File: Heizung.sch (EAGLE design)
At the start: 32 parts, among them IC1 MEGA8-PTQFP, Q2 2N7002, Q3 2N7002

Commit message: change min width to 3.5mm, fix XTAL
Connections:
- new net N$41: J_1.1, J_2.1, J_3.1, J_4.1
- net GND: no longer J_1.1, J_2.1, J_3.1, J_4.1
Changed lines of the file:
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@@
 <grid distance="0.1" unitdist="inch" unit="inch" style="lines" multiple="1" display="no" altdistance="0.01" altunitdist="inch" altunit="inch"/>
 <layers>
-<layer number="1" name="Top" color="4" fill="1" visible="no" active="no"/>
-<layer number="16" name="Bottom" color="1" fill="1" visible="no" active="no"/>
-<layer number="17" name="Pads" color="2" fill="1" visible="no" active="no"/>
-<layer number="18" name="Vias" color="2" fill="1" visible="no" active="no"/>
-<layer number="19" name="Unrouted" color="6" fill="1" visible="no" active="no"/>
-<layer number="20" name="Dimension" color="15" fill="1" visible="no" active="no"/>
-<layer number="21" name="tPlace" color="7" fill="1" visible="no" active="no"/>
-<layer number="22" name="bPlace" color="7" fill="1" visible="no" active="no"/>
-<layer number="23" name="tOrigins" color="15" fill="1" visible="no" active="no"/>
-<layer number="24" name="bOrigins" color="15" fill="1" visible="no" active="no"/>
-<layer number="25" name="tNames" color="7" fill="1" visible="no" active="no"/>
-<layer number="26" name="bNames" color="7" fill="1" visible="no" active="no"/>
-<layer number="27" name="tValues" color="7" fill="1" visible="no" active="no"/>
-<layer number="28" name="bValues" color="7" fill="1" visible="no" active="no"/>
+<layer number="1" name="Top" color="4" fill="1" visible="yes" active="no"/>
+<layer number="16" name="Bottom" color="1" fill="1" visible="yes" active="no"/>
+<layer number="17" name="Pads" color="2" fill="1" visible="yes" active="no"/>
+<layer number="18" name="Vias" color="2" fill="1" visible="yes" active="no"/>
+<layer number="19" name="Unrouted" color="6" fill="1" visible="yes" active="no"/>
+<layer number="20" name="Dimension" color="15" fill="1" visible="yes" active="no"/>
+<layer number="21" name="tPlace" color="7" fill="1" visible="yes" active="no"/>
+<layer number="22" name="bPlace" color="7" fill="1" visible="yes" active="no"/>
+<layer number="23" name="tOrigins" color="15" fill="1" visible="yes" active="no"/>
+<layer number="24" name="bOrigins" color="15" fill="1" visible="yes" active="no"/>
+<layer number="25" name="tNames" color="7" fill="1" visible="yes" active="no"/>
+<layer number="26" name="bNames" color="7" fill="1" visible="yes" active="no"/>
+<layer number="27" name="tValues" color="7" fill="1" visible="yes" active="no"/>
+<layer number="28" name="bValues" color="7" fill="1" visible="yes" active="no"/>
 <layer number="29" name="tStop" color="7" fill="3" visible="no" active="no"/>
 <layer number="30" name="bStop" color="7" fill="6" visible="no" active="no"/>
@@
 <layer number="35" name="tGlue" color="7" fill="4" visible="no" active="no"/>
 <layer number="36" name="bGlue" color="7" fill="5" visible="no" active="no"/>
-<layer number="37" name="tTest" color="7" fill="1" visible="no" active="no"/>
-<layer number="38" name="bTest" color="7" fill="1" visible="no" active="no"/>
+<layer number="37" name="tTest" color="7" fill="1" visible="yes" active="no"/>
+<layer number="38" name="bTest" color="7" fill="1" visible="yes" active="no"/>
 <layer number="39" name="tKeepout" color="4" fill="11" visible="no" active="no"/>
 <layer number="40" name="bKeepout" color="1" fill="11" visible="no" active="no"/>
@@
 <layer number="44" name="Drills" color="7" fill="1" visible="no" active="no"/>
 <layer number="45" name="Holes" color="7" fill="1" visible="no" active="no"/>
-<layer number="46" name="Milling" color="3" fill="1" visible="no" active="no"/>
-<layer number="47" name="Measures" color="7" fill="1" visible="no" active="no"/>
-<layer number="48" name="Document" color="7" fill="1" visible="no" active="no"/>
-<layer number="49" name="Reference" color="7" fill="1" visible="no" active="no"/>
-<layer number="50" name="dxf" color="7" fill="1" visible="no" active="no"/>
-<layer number="51" name="tDocu" color="7" fill="1" visible="no" active="no"/>
-<layer number="52" name="bDocu" color="7" fill="1" visible="no" active="no"/>
-<layer number="53" name="tGND_GNDA" color="7" fill="9" visible="no" active="no"/>
-<layer number="54" name="bGND_GNDA" color="1" fill="9" visible="no" active="no"/>
-<layer number="56" name="wert" color="7" fill="1" visible="no" active="no"/>
-<layer number="57" name="tCAD" color="7" fill="1" visible="no" active="no"/>
+<layer number="46" name="Milling" color="3" fill="1" visible="yes" active="no"/>
+<layer number="47" name="Measures" color="7" fill="1" visible="yes" active="no"/>
+<layer number="48" name="Document" color="7" fill="1" visible="yes" active="no"/>
+<layer number="49" name="Reference" color="7" fill="1" visible="yes" active="no"/>
+<layer number="50" name="dxf" color="7" fill="1" visible="yes" active="no"/>
+<layer number="51" name="tDocu" color="7" fill="1" visible="yes" active="no"/>
+<layer number="52" name="bDocu" color="7" fill="1" visible="yes" active="no"/>
+<layer number="53" name="tGND_GNDA" color="7" fill="9" visible="yes" active="no"/>
+<layer number="54" name="bGND_GNDA" color="1" fill="9" visible="yes" active="no"/>
+<layer number="56" name="wert" color="7" fill="1" visible="yes" active="no"/>
+<layer number="57" name="tCAD" color="7" fill="1" visible="yes" active="no"/>
 <layer number="90" name="Modules" color="5" fill="1" visible="yes" active="yes"/>
 <layer number="91" name="Nets" color="2" fill="1" visible="yes" active="yes"/>
@@
 <junction x="63.5" y="78.74"/>
 <pinref part="GND_" gate="G$1" pin="1"/>
-<wire x1="142.24" y1="81.28" x2="142.24" y2="88.9" width="0.1524" layer="91"/>
+<wire x1="142.24" y1="78.74" x2="142.24" y2="88.9" width="0.1524" layer="91"/>
 <pinref part="GND1" gate="G$1" pin="1"/>
 <wire x1="142.24" y1="88.9" x2="142.24" y2="106.68" width="0.1524" layer="91"/>
@@
 <wire x1="20.32" y1="99.06" x2="12.7" y2="99.06" width="0.1524" layer="91"/>
 <junction x="12.7" y="99.06"/>
-<wire x1="142.24" y1="78.74" x2="142.24" y2="81.28" width="0.1524" layer="91"/>
-<wire x1="142.24" y1="81.28" x2="165.1" y2="81.28" width="0.1524" layer="91"/>
-<pinref part="J_4" gate="G$1" pin="1"/>
-<wire x1="165.1" y1="81.28" x2="165.1" y2="76.2" width="0.1524" layer="91"/>
-<wire x1="165.1" y1="76.2" x2="170.18" y2="76.2" width="0.1524" layer="91"/>
-<pinref part="J_3" gate="G$1" pin="1"/>
-<wire x1="165.1" y1="81.28" x2="165.1" y2="91.44" width="0.1524" layer="91"/>
-<wire x1="165.1" y1="91.44" x2="170.18" y2="91.44" width="0.1524" layer="91"/>
-<junction x="165.1" y="81.28"/>
-<pinref part="J_2" gate="G$1" pin="1"/>
-<wire x1="165.1" y1="91.44" x2="165.1" y2="106.68" width="0.1524" layer="91"/>
-<wire x1="165.1" y1="106.68" x2="170.18" y2="106.68" width="0.1524" layer="91"/>
-<junction x="165.1" y="91.44"/>
-<pinref part="J_1" gate="G$1" pin="1"/>
-<wire x1="165.1" y1="106.68" x2="165.1" y2="121.92" width="0.1524" layer="91"/>
-<wire x1="165.1" y1="121.92" x2="170.18" y2="121.92" width="0.1524" layer="91"/>
-<junction x="165.1" y="106.68"/>
 </segment>
 </net>
@@
 <wire x1="132.08" y1="127" x2="137.16" y2="127" width="0.1524" layer="91"/>
 <junction x="132.08" y="127"/>
-<wire x1="137.16" y1="127" x2="157.48" y2="127" width="0.1524" layer="91"/>
-<wire x1="157.48" y1="127" x2="157.48" y2="81.28" width="0.1524" layer="91"/>
-<wire x1="157.48" y1="81.28" x2="162.56" y2="81.28" width="0.1524" layer="91"/>
 <pinref part="R5" gate="G$1" pin="2"/>
 <pinref part="R6" gate="G$1" pin="2"/>
@@
 <wire x1="137.16" y1="99.06" x2="137.16" y2="127" width="0.1524" layer="91"/>
 <junction x="137.16" y="99.06"/>
-<junction x="137.16" y="127"/>
 </segment>
 </net>
@@
 </segment>
 </net>
+<net name="N$41" class="1">
+<segment>
+<pinref part="J_1" gate="G$1" pin="1"/>
+<wire x1="165.1" y1="121.92" x2="170.18" y2="121.92" width="0.1524" layer="91"/>
+<pinref part="J_2" gate="G$1" pin="1"/>
+<wire x1="165.1" y1="106.68" x2="170.18" y2="106.68" width="0.1524" layer="91"/>
+<wire x1="165.1" y1="106.68" x2="165.1" y2="121.92" width="0.1524" layer="91"/>
+<junction x="165.1" y="106.68"/>
+<pinref part="J_3" gate="G$1" pin="1"/>
+<pinref part="J_4" gate="G$1" pin="1"/>
+<wire x1="165.1" y1="76.2" x2="170.18" y2="76.2" width="0.1524" layer="91"/>
+<wire x1="165.1" y1="76.2" x2="165.1" y2="91.44" width="0.1524" layer="91"/>
+<wire x1="165.1" y1="91.44" x2="170.18" y2="91.44" width="0.1524" layer="91"/>
+<wire x1="165.1" y1="91.44" x2="165.1" y2="106.68" width="0.1524" layer="91"/>
+<junction x="165.1" y="91.44"/>
+</segment>
+</net>
 </nets>
 </sheet>
 </sheets>
+<errors>
+</errors>
 </schematic>
 </drawing>

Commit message: Floating wires are bad for you
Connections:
- removed net N$41: J_1.1, J_2.1, J_3.1, J_4.1
- net GND: now also J_1.1, J_2.1, J_3.1, J_4.1
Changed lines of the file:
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@@
 <junction x="12.7" y="99.06"/>
+</segment>
+<segment>
+<pinref part="J_1" gate="G$1" pin="1"/>
+<wire x1="165.1" y1="121.92" x2="170.18" y2="121.92" width="0.1524" layer="91"/>
+<pinref part="J_2" gate="G$1" pin="1"/>
+<wire x1="165.1" y1="106.68" x2="170.18" y2="106.68" width="0.1524" layer="91"/>
+<wire x1="165.1" y1="106.68" x2="165.1" y2="121.92" width="0.1524" layer="91"/>
+<junction x="165.1" y="106.68"/>
+<pinref part="J_3" gate="G$1" pin="1"/>
+<pinref part="J_4" gate="G$1" pin="1"/>
+<wire x1="165.1" y1="76.2" x2="170.18" y2="76.2" width="0.1524" layer="91"/>
+<wire x1="165.1" y1="76.2" x2="165.1" y2="91.44" width="0.1524" layer="91"/>
+<wire x1="165.1" y1="91.44" x2="170.18" y2="91.44" width="0.1524" layer="91"/>
+<wire x1="165.1" y1="91.44" x2="165.1" y2="106.68" width="0.1524" layer="91"/>
+<junction x="165.1" y="91.44"/>
 </segment>
 </net>
@@
 </segment>
 </net>
-<net name="N$41" class="1">
-<segment>
-<pinref part="J_1" gate="G$1" pin="1"/>
-<wire x1="165.1" y1="121.92" x2="170.18" y2="121.92" width="0.1524" layer="91"/>
-<pinref part="J_2" gate="G$1" pin="1"/>
-<wire x1="165.1" y1="106.68" x2="170.18" y2="106.68" width="0.1524" layer="91"/>
-<wire x1="165.1" y1="106.68" x2="165.1" y2="121.92" width="0.1524" layer="91"/>
-<junction x="165.1" y="106.68"/>
-<pinref part="J_3" gate="G$1" pin="1"/>
-<pinref part="J_4" gate="G$1" pin="1"/>
-<wire x1="165.1" y1="76.2" x2="170.18" y2="76.2" width="0.1524" layer="91"/>
-<wire x1="165.1" y1="76.2" x2="165.1" y2="91.44" width="0.1524" layer="91"/>
-<wire x1="165.1" y1="91.44" x2="170.18" y2="91.44" width="0.1524" layer="91"/>
-<wire x1="165.1" y1="91.44" x2="165.1" y2="106.68" width="0.1524" layer="91"/>
-<junction x="165.1" y="91.44"/>
-</segment>
-</net>

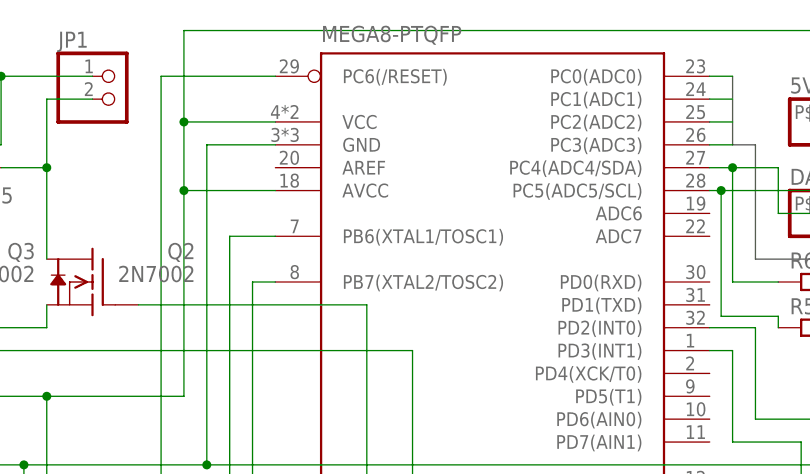
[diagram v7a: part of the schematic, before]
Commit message: V2.9
add capacitor to AREF
better routing
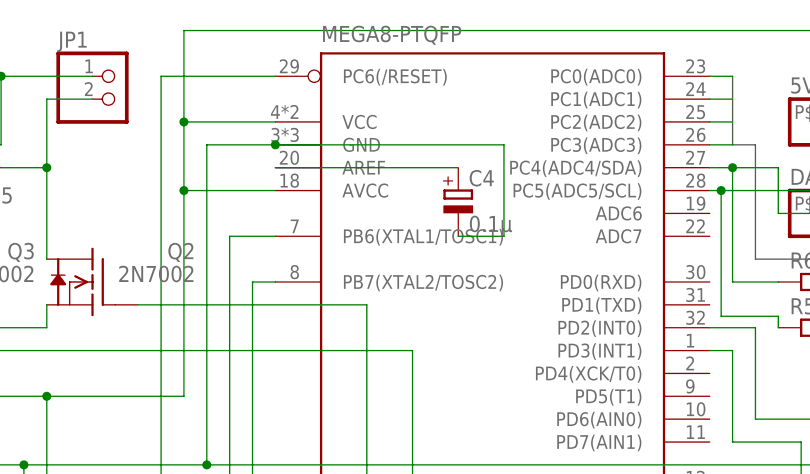
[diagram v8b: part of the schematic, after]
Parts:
- added C4: 0.1µ, common:CP1206
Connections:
- new net N$41: C4.+, IC1.AREF
- net GND: now also C4.-
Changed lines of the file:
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@@
 <grid distance="0.1" unitdist="inch" unit="inch" style="lines" multiple="1" display="no" altdistance="0.01" altunitdist="inch" altunit="inch"/>
 <layers>
-<layer number="1" name="Top" color="4" fill="1" visible="yes" active="no"/>
-<layer number="16" name="Bottom" color="1" fill="1" visible="yes" active="no"/>
-<layer number="17" name="Pads" color="2" fill="1" visible="yes" active="no"/>
-<layer number="18" name="Vias" color="2" fill="1" visible="yes" active="no"/>
-<layer number="19" name="Unrouted" color="6" fill="1" visible="yes" active="no"/>
-<layer number="20" name="Dimension" color="15" fill="1" visible="yes" active="no"/>
-<layer number="21" name="tPlace" color="7" fill="1" visible="yes" active="no"/>
-<layer number="22" name="bPlace" color="7" fill="1" visible="yes" active="no"/>
-<layer number="23" name="tOrigins" color="15" fill="1" visible="yes" active="no"/>
-<layer number="24" name="bOrigins" color="15" fill="1" visible="yes" active="no"/>
-<layer number="25" name="tNames" color="7" fill="1" visible="yes" active="no"/>
-<layer number="26" name="bNames" color="7" fill="1" visible="yes" active="no"/>
-<layer number="27" name="tValues" color="7" fill="1" visible="yes" active="no"/>
-<layer number="28" name="bValues" color="7" fill="1" visible="yes" active="no"/>
+<layer number="1" name="Top" color="4" fill="1" visible="no" active="no"/>
+<layer number="16" name="Bottom" color="1" fill="1" visible="no" active="no"/>
+<layer number="17" name="Pads" color="2" fill="1" visible="no" active="no"/>
+<layer number="18" name="Vias" color="2" fill="1" visible="no" active="no"/>
+<layer number="19" name="Unrouted" color="6" fill="1" visible="no" active="no"/>
+<layer number="20" name="Dimension" color="15" fill="1" visible="no" active="no"/>
+<layer number="21" name="tPlace" color="7" fill="1" visible="no" active="no"/>
+<layer number="22" name="bPlace" color="7" fill="1" visible="no" active="no"/>
+<layer number="23" name="tOrigins" color="15" fill="1" visible="no" active="no"/>
+<layer number="24" name="bOrigins" color="15" fill="1" visible="no" active="no"/>
+<layer number="25" name="tNames" color="7" fill="1" visible="no" active="no"/>
+<layer number="26" name="bNames" color="7" fill="1" visible="no" active="no"/>
+<layer number="27" name="tValues" color="7" fill="1" visible="no" active="no"/>
+<layer number="28" name="bValues" color="7" fill="1" visible="no" active="no"/>
 <layer number="29" name="tStop" color="7" fill="3" visible="no" active="no"/>
 <layer number="30" name="bStop" color="7" fill="6" visible="no" active="no"/>
@@
 <layer number="35" name="tGlue" color="7" fill="4" visible="no" active="no"/>
 <layer number="36" name="bGlue" color="7" fill="5" visible="no" active="no"/>
-<layer number="37" name="tTest" color="7" fill="1" visible="yes" active="no"/>
-<layer number="38" name="bTest" color="7" fill="1" visible="yes" active="no"/>
+<layer number="37" name="tTest" color="7" fill="1" visible="no" active="no"/>
+<layer number="38" name="bTest" color="7" fill="1" visible="no" active="no"/>
 <layer number="39" name="tKeepout" color="4" fill="11" visible="no" active="no"/>
 <layer number="40" name="bKeepout" color="1" fill="11" visible="no" active="no"/>
@@
 <layer number="44" name="Drills" color="7" fill="1" visible="no" active="no"/>
 <layer number="45" name="Holes" color="7" fill="1" visible="no" active="no"/>
-<layer number="46" name="Milling" color="3" fill="1" visible="yes" active="no"/>
-<layer number="47" name="Measures" color="7" fill="1" visible="yes" active="no"/>
-<layer number="48" name="Document" color="7" fill="1" visible="yes" active="no"/>
-<layer number="49" name="Reference" color="7" fill="1" visible="yes" active="no"/>
-<layer number="50" name="dxf" color="7" fill="1" visible="yes" active="no"/>
-<layer number="51" name="tDocu" color="7" fill="1" visible="yes" active="no"/>
-<layer number="52" name="bDocu" color="7" fill="1" visible="yes" active="no"/>
-<layer number="53" name="tGND_GNDA" color="7" fill="9" visible="yes" active="no"/>
-<layer number="54" name="bGND_GNDA" color="1" fill="9" visible="yes" active="no"/>
-<layer number="56" name="wert" color="7" fill="1" visible="yes" active="no"/>
-<layer number="57" name="tCAD" color="7" fill="1" visible="yes" active="no"/>
+<layer number="46" name="Milling" color="3" fill="1" visible="no" active="no"/>
+<layer number="47" name="Measures" color="7" fill="1" visible="no" active="no"/>
+<layer number="48" name="Document" color="7" fill="1" visible="no" active="no"/>
+<layer number="49" name="Reference" color="7" fill="1" visible="no" active="no"/>
+<layer number="50" name="dxf" color="7" fill="1" visible="no" active="no"/>
+<layer number="51" name="tDocu" color="7" fill="1" visible="no" active="no"/>
+<layer number="52" name="bDocu" color="7" fill="1" visible="no" active="no"/>
+<layer number="53" name="tGND_GNDA" color="7" fill="9" visible="no" active="no"/>
+<layer number="54" name="bGND_GNDA" color="1" fill="9" visible="no" active="no"/>
+<layer number="56" name="wert" color="7" fill="1" visible="no" active="no"/>
+<layer number="57" name="tCAD" color="7" fill="1" visible="no" active="no"/>
 <layer number="90" name="Modules" color="5" fill="1" visible="yes" active="yes"/>
 <layer number="91" name="Nets" color="2" fill="1" visible="yes" active="yes"/>
@@
 </variantdefs>
 <classes>
-<class number="0" name="default" width="0" drill="0">
+<class number="0" name="default" width="0.35" drill="0">
 </class>
 <class number="1" name="wires" width="0.5" drill="0">
@@
 <part name="J_4" library="common" deviceset="PINHD-1X2" device="LEVER"/>
 <part name="D4" library="common" deviceset="BAS40-05" device=""/>
+<part name="C4" library="common" deviceset="CP" device="1206" value="0.1µ"/>
 </parts>
 <sheets>
@@
 <instance part="J_4" gate="G$1" x="172.72" y="73.66"/>
 <instance part="D4" gate="G$1" x="35.56" y="111.76"/>
+<instance part="C4" gate="G$1" x="91.44" y="109.22"/>
 </instances>
 <busses>
@@
 <wire x1="20.32" y1="99.06" x2="12.7" y2="99.06" width="0.1524" layer="91"/>
 <junction x="12.7" y="99.06"/>
+<wire x1="71.12" y1="114.3" x2="96.52" y2="114.3" width="0.1524" layer="91"/>
+<junction x="71.12" y="114.3"/>
+<wire x1="96.52" y1="114.3" x2="96.52" y2="104.14" width="0.1524" layer="91"/>
+<pinref part="C4" gate="G$1" pin="-"/>
+<wire x1="96.52" y1="104.14" x2="91.44" y2="104.14" width="0.1524" layer="91"/>
 </segment>
 <segment>
@@
 </segment>
 </net>
+<net name="N$41" class="0">
+<segment>
+<pinref part="IC1" gate="G$1" pin="AREF"/>
+<pinref part="C4" gate="G$1" pin="+"/>
+<wire x1="71.12" y1="111.76" x2="91.44" y2="111.76" width="0.1524" layer="91"/>
+</segment>
+</net>
